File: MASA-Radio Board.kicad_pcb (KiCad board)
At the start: 4 copper layers, 75.8 x 76.2 mm, 71 parts, among them IC1 FAN4010IL6X_F113, IC2 FAN4010IL6X_F113, J1 Conn_01x02, J2 Conn_01x02_Male, J3 Conn_01x02_Male, J4 Conn_01x03_Male, J5 Conn_01x06, J6 SC_19-20, J7 Conn_01x06, J8 Conn_01x02, J9 UJ2-MBH-1-SMT-TR, U1 MP5077GG-Z, U2 BL654PA, U3 MIC5504-3.3YM5, U4 MP5077GG-Z, U5 SN74LVC1T45DBVR, U6 SN65HVD1050D, U7 MCP2515-xSO, U8 SN74LVC1T45DBVR

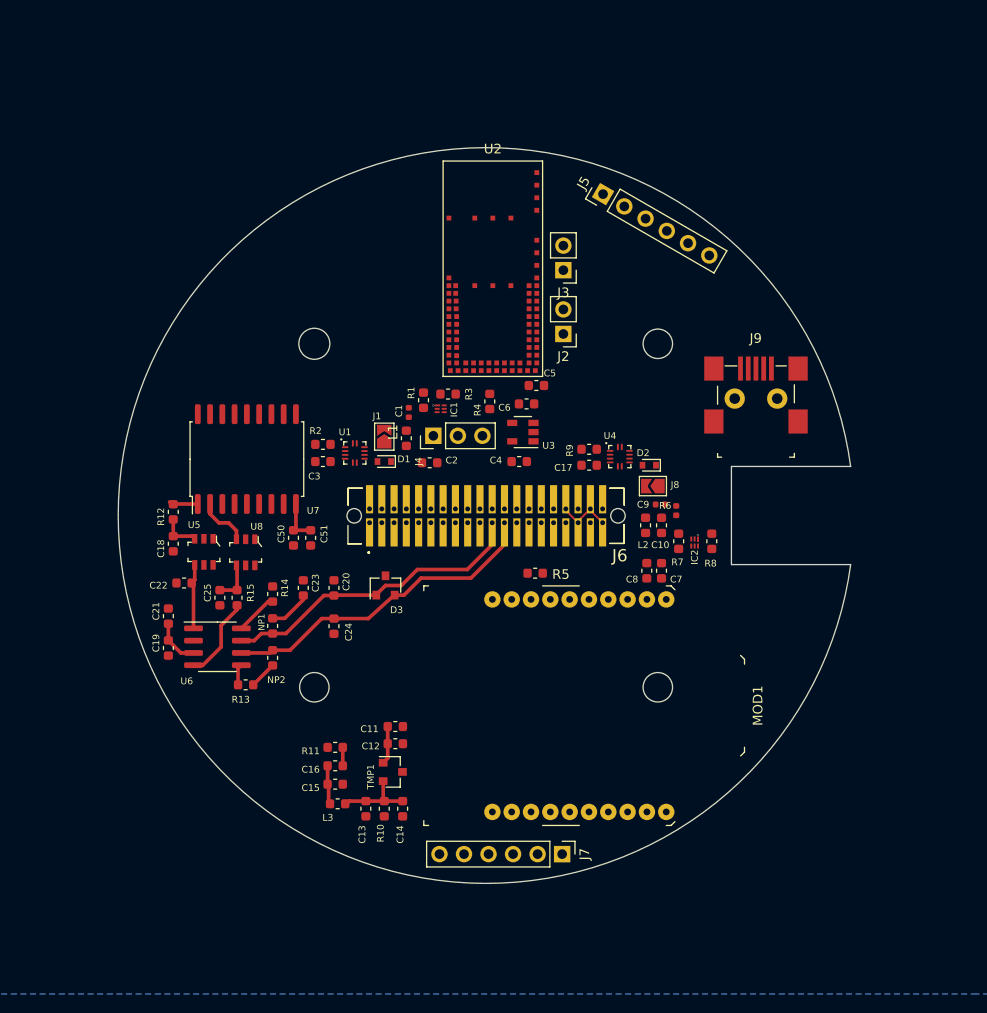
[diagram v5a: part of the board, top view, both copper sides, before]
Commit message: Completed Most of the routing on board
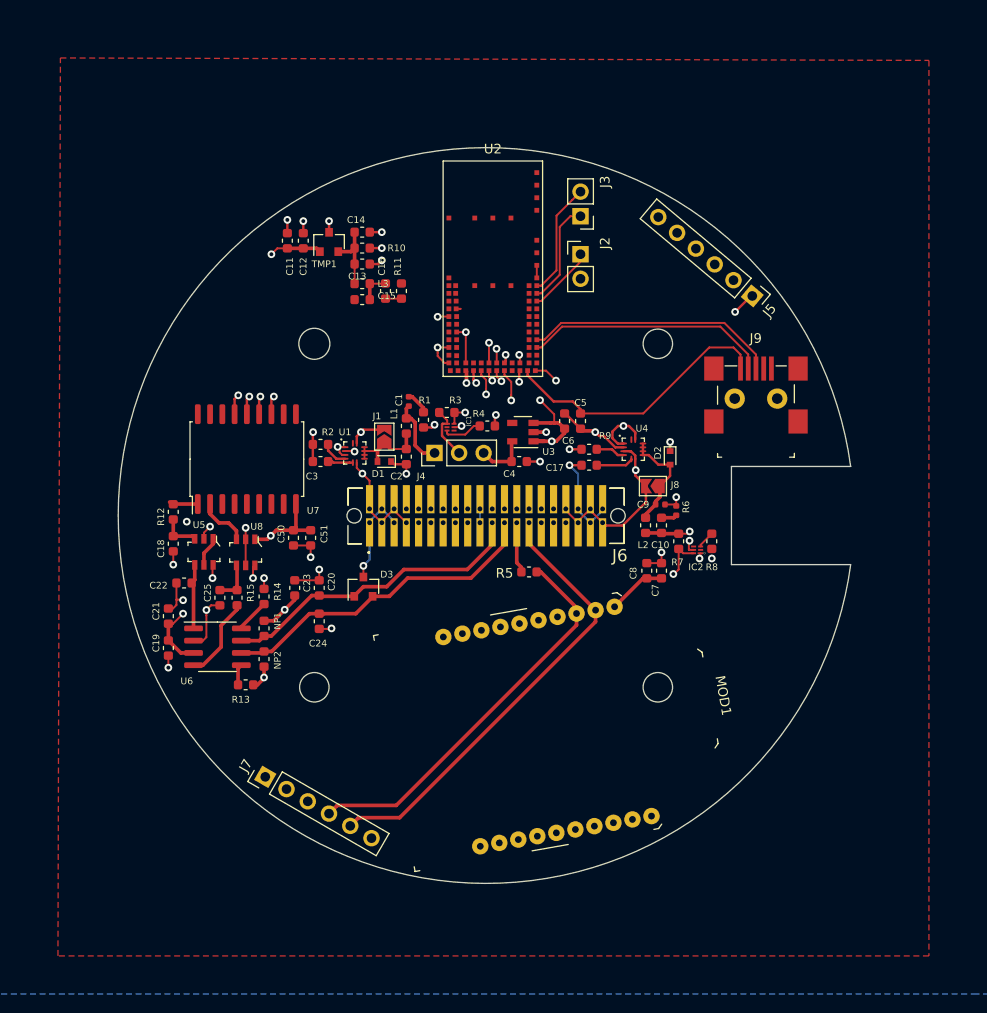
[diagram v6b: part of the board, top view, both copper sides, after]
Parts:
- moved C14 59.8 mm to (139.6, 97.7), turned to 0 degrees
- moved R10 58.1 mm to (139.6, 99.3), turned to 0 degrees
- moved C13 56.4 mm to (139.6, 101.0), turned to 0 degrees
- moved TMP1 55.3 mm to (136.1, 98.7), turned to 90 degrees
- moved L3 53.9 mm to (139.6, 103.0), turned to 0 degrees
- moved C12 52.9 mm to (133.5, 98.6), turned to 90 degrees
- moved C11 51.5 mm to (131.8, 98.6), turned to 90 degrees
- moved C15 50.2 mm to (139.6, 104.6), turned to 180 degrees
- moved C16 49.4 mm to (142.0, 103.8), turned to 270 degrees
- moved R11 47.7 mm to (143.6, 103.8), turned to 270 degrees
- moved J7 31.8 mm to (129.5, 154.1), turned to 60 degrees
- moved J5 18.7 mm to (180.0, 104.3), turned to 230 degrees
- moved J2 8.44 mm to (162.2, 99.9), turned to 0 degrees
- moved C5 5.87 mm to (162.2, 117.2), turned to 270 degrees
- moved J3 5.86 mm to (162.2, 96.0)
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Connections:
- J2 pad 2: Net-(J2-Pad2) -> +3V3
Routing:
- net V_IN_5V0: track 0.00 -> 113.1 mm, vias 0 -> 2
- net GND: track 0.03 -> 107.4 mm, vias 0 -> 41
- net +5V: track 8.81 -> 109.1 mm, vias 0 -> 5
- net 5V0: track 5.87 -> 60.1 mm, vias 0 -> 3
- net XBee_TX: track 0.00 -> 47.3 mm
- net XBee_RX: track 0.00 -> 41.2 mm
- net UART_RTS: track 0.00 -> 35.7 mm, vias 0 -> 1
- net SPI_MISO: track 0.00 -> 32.4 mm, vias 0 -> 2
- net SPI_MOSI: track 0.00 -> 31.1 mm, vias 0 -> 2
- net MCU_TX: track 0.00 -> 30.2 mm, vias 0 -> 1
- net UART_CTS: track 0.00 -> 30.1 mm, vias 0 -> 1
- net SPI_CLK: track 0.00 -> 30.0 mm, vias 0 -> 2
- net USB_VBUS: track 0.00 -> 29.0 mm
- net MCU_RX: track 0.00 -> 29.0 mm, vias 0 -> 1
- net USB_D+: track 0.00 -> 26.2 mm
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- added copper zone on F.Cu, net GND
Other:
- net class Default: clearance 0.2 -> 0.127
- rule pad_to_mask_clearance: 0.051 -> 0.0508
- rule solder_mask_min_width: 0.25 -> 0.1524
- rule trace_clearance: 0.2 -> 0.127
- rule trace_min: 0.1524 -> 0.1016

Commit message: Some small routing changes
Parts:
- moved J2 0.44 mm to (162.2, 99.5)
- moved J3 0.38 mm to (162.2, 95.6)
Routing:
- net USB_VBUS: track 29.0 -> 39.8 mm
- net USB_D+: track 26.2 -> 30.1 mm
- net USB_D-: track 25.4 -> 29.3 mm
- net +3V3: track 22.9 -> 25.6 mm, vias 4 -> 5
- net nAutoRun: track 6.99 -> 8.05 mm
- net GND: track 107.4 -> 107.8 mm, vias 41 -> 58
- net +5V: vias 5 -> 6

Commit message: Some I/O routing
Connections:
- U2 pad 41: Net-(U2-Pad41) -> RX1BF
- U2 pad 42: Net-(U2-Pad42) -> RX0BF
- U2 pad 49: Net-(U2-Pad49) -> TX1RTS
- U2 pad 50: Net-(U2-Pad50) -> TX2RTS
- U2 pad 51: Net-(U2-Pad51) -> TX0RTS
- U2 pad 53: Net-(U2-Pad53) -> CAN_INT
- U2 pad 56: Net-(U2-Pad56) -> CS
- U2 pad 57: Net-(U2-Pad57) -> CAN_RST
- U2 pad 63: Net-(U2-Pad63) -> TSENSE
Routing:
- net CS: track 0.00 -> 36.5 mm, vias 0 -> 2
- net CAN_RST: track 0.00 -> 34.3 mm
- net TX2RTS: track 0.00 -> 32.3 mm, vias 0 -> 4
- net TX0RTS: track 0.00 -> 31.0 mm, vias 0 -> 2
- net TX1RTS: track 0.00 -> 30.1 mm, vias 0 -> 2
- net CAN_INT: track 1.93 -> 23.2 mm, vias 1 -> 2
- net RX0BF: track 0.00 -> 20.0 mm
- net RX1BF: track 0.00 -> 18.9 mm
- net TSENSE: track 3.29 -> 11.2 mm
- net GND: track 107.8 -> 106.6 mm, vias 58 -> 59
